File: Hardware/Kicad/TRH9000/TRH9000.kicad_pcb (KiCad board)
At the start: 2 copper layers, 99.1 x 63.5 mm, 74 parts, among them J1 RGB, J2 Console5_SCART, Q1 BC817, U1 V9990, U2 KM428C256, U3 KM428C256, U4 74VHC138, U5 T.I_SN74AHCT32D, U6 LMH1980, U7 T.I_SN74AHCT32D, X1 Crystek_CE3291, Y1 21.47727Mhz

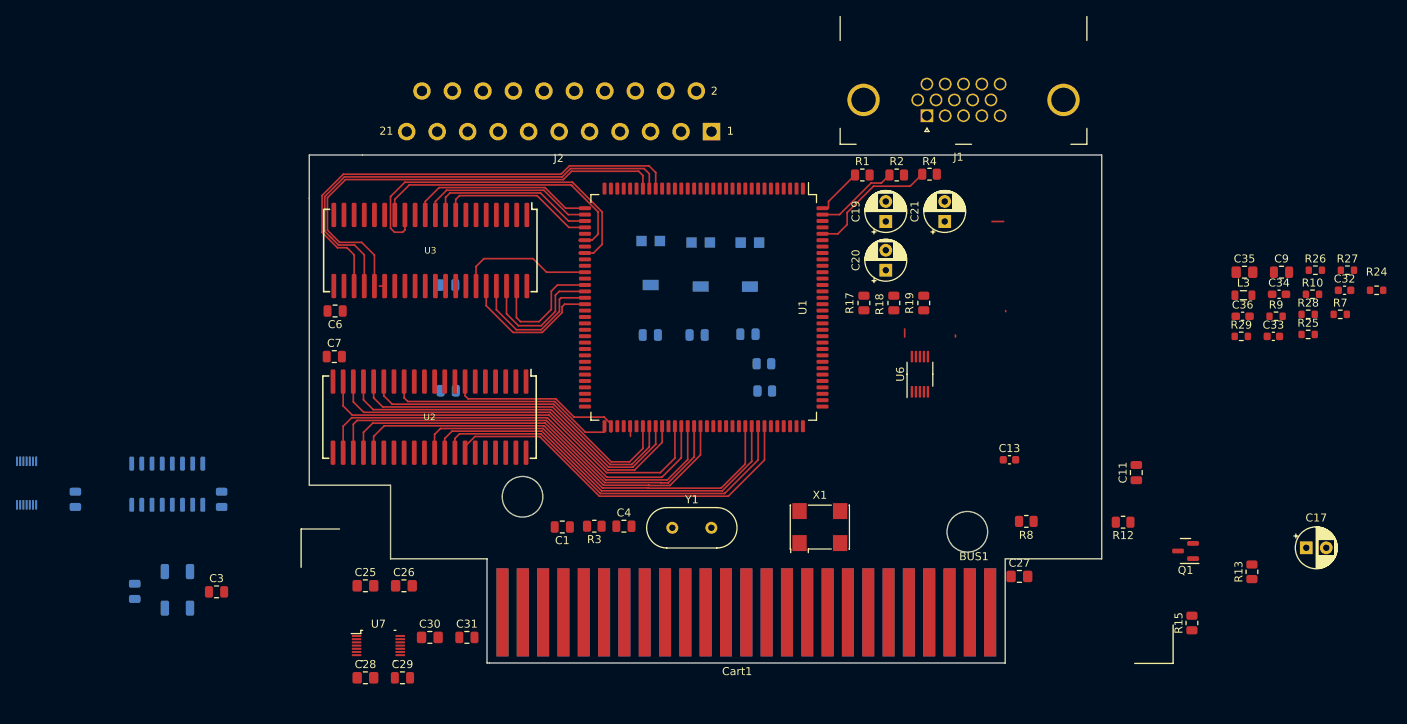
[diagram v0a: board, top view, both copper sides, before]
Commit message: Started routing the PCB, adding cut-outs to separate the analog from digital signal-domains.
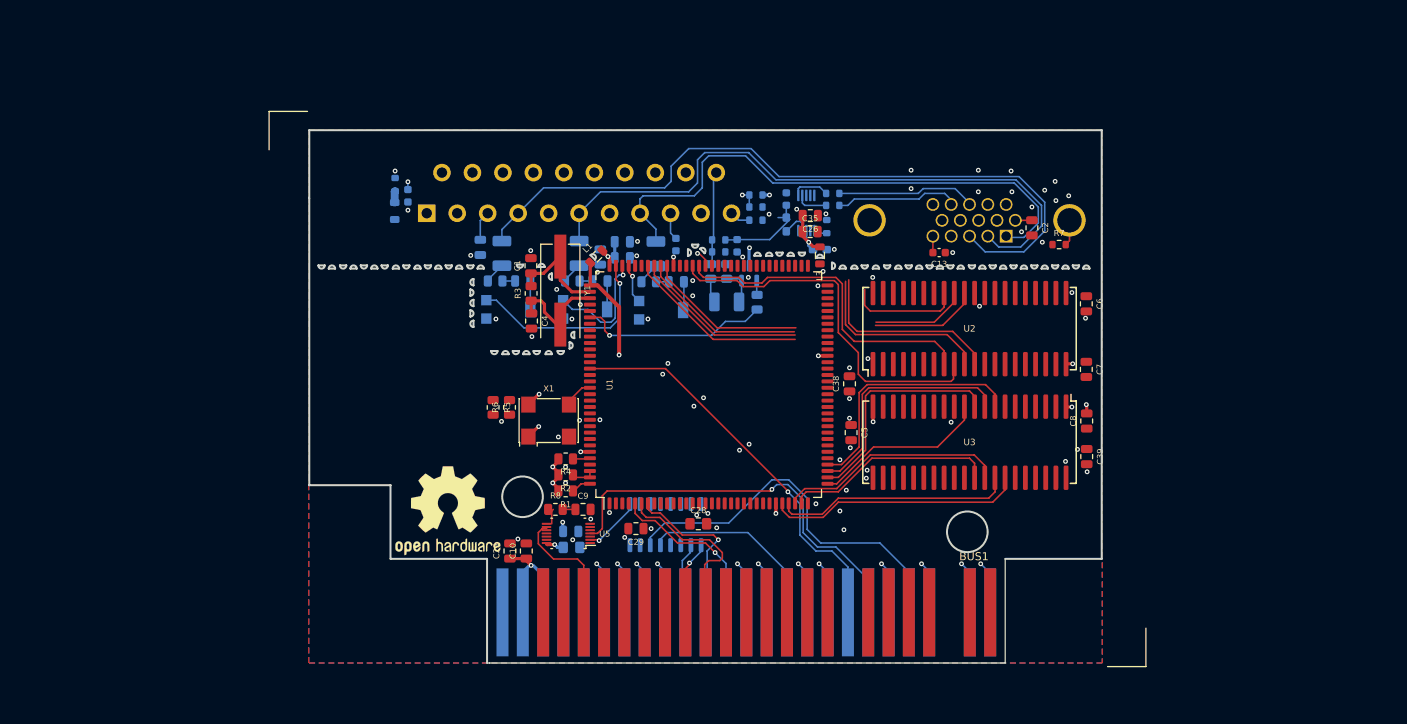
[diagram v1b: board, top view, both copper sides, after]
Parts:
- removed C11, C12: C_CC0805JPX7R9BB104, Capacitor_SMD:C_0805_2012Metric
- removed U7: T.I_SN74AHCT32D, trh9000:Texas_R-PDSO-G14_3.6x4.4mm
- added C23: C_CL21B106KOQNNNE, Capacitor_SMD:C_0805_2012Metric, F.Cu at (123.3, 113.0)
- added C24: C_CC0805JPX7R9BB104, Capacitor_SMD:C_0805_2012Metric, B.Cu at (119.7, 75.0)
- added C37: C_CC0805JPX7R9BB104, Capacitor_SMD:C_0805_2012Metric, B.Cu at (137.4, 74.3)
- added C38: C_CL21B106KOQNNNE, Capacitor_SMD:C_0805_2012Metric, F.Cu at (165.8, 92.1)
- added C39: C_CL21B106KOQNNNE, Capacitor_SMD:C_0805_2012Metric, F.Cu at (195.4, 101.2)
- added C40: 47pF, Capacitor_SMD:C_0603_1608Metric, B.Cu at (144.1, 74.7)
- added LOGO1: Logo_Open_Hardware_Small, Symbol:OSHW-Logo2_14.6x12mm_SilkScreen, F.Cu at (115.6, 108.0)
- added R11: R_ERJ-3GEYJ105V, Resistor_SMD:R_0603_1608Metric, B.Cu at (154.1, 71.7)
- BUS1: value MSX_SLOT_EDGE-CON -> MSX-CONN_L-P; footprint trh9000:msx_cartridge -> trh9000:msx_edge-conn-LP
- C10, C5, C8, R5, R6, U5: moved to F.Cu
- C17, C19, C20, C21: value 220uF -> C_TCJB227; footprint Capacitor_THT:CP_Radial_D5.0mm_P2.50mm -> Capacitor_Tantalum_SMD:CP_EIA-3528-15_AVX-H; moved to B.Cu
- C2: value 100nF -> C_CC0805JPX7R9BB104; moved to F.Cu
- C25: value C_CL21B105KBFNNNF -> C_GRM188D71A106KA73D; footprint Capacitor_SMD:C_0805_2012Metric_Pad1.18x1.45mm_HandSolder -> Capacitor_SMD:C_0603_1608Metric; moved to B.Cu
- C26: value C_CL21B105KBFNNNF -> 10nF; footprint Capacitor_SMD:C_0805_2012Metric_Pad1.18x1.45mm_HandSolder -> Capacitor_SMD:C_0805_2012Metric
- C27: value C_CL21B105KBFNNNF -> 10nF; footprint Capacitor_SMD:C_0805_2012Metric_Pad1.18x1.45mm_HandSolder -> Capacitor_SMD:C_0805_2012Metric; moved to B.Cu
- C3, C30, C31, C32, C33, C34, C36, J1, J2, Q1, R10, R12, R13, R15, R17, R18, R19, R24, R25, R26, R27, R28, R29, R9, U6: moved to B.Cu
- C35: value C_GRM21BR71A106KA73K -> C_CL21B106KOQNNNE; footprint Capacitor_SMD:C_0805_2012Metric_Pad1.18x1.45mm_HandSolder -> Capacitor_SMD:C_0805_2012Metric
- Cart1: footprint trh9000:MSX-cart-dummy -> trh9000:MSX-cart-dummy_RA
- L1: value 4.7uH -> L_MLZ2012M4R7HT000; footprint Inductor_SMD:L_1206_3216Metric -> Inductor_SMD:L_0805_2012Metric; moved to F.Cu
- L2: value 4.7uH -> L_MLZ2012M4R7HT000; footprint Inductor_SMD:L_1206_3216Metric -> Inductor_SMD:L_0805_2012Metric
- Y1: value 21.47727Mhz -> Y_HCM4921477270ABJT; footprint Crystal:Crystal_HC49-U_Vertical -> LRJ:Crystal_HC49-US_Vertical
- moved C2 121.0 mm to (188.6, 72.6), turned to -90 degrees
- moved R29 107.5 mm to (109.0, 67.2), turned to -90 degrees
- moved C7 94.0 mm to (195.4, 90.3), turned to -90 degrees
- moved C6 93.9 mm to (195.4, 82.1), turned to -90 degrees
- moved C9 92.2 mm to (132.5, 107.8)
- moved C8 79.9 mm to (195.4, 96.8), turned to 90 degrees
- moved C17 78.7 mm to (150.4, 81.9), turned to 180 degrees
- moved C32 76.1 mm to (151.8, 74.8), turned to -90 degrees
- moved R13 75.6 mm to (150.4, 78.1)
- moved R27 74.5 mm to (154.1, 68.5), turned to 180 degrees
- moved R10 74.5 mm to (149.4, 74.1), turned to 180 degrees
- moved R15 74.5 mm to (148.4, 78.1), turned to -90 degrees
- moved U3 71.5 mm to (180.8, 99.4)
- moved R28 70.3 mm to (154.1, 70.0)
- moved R9 70.1 mm to (149.4, 75.6)
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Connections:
- net /VDP/X1 renamed /VDP/X+
- net /VDP/X2 renamed /VDP/X-
- net /VIDEO/2.5V renamed /VIDEO/2.5VA
- net /VIDEO/SYNCIN renamed /VIDEO/Csync_
- net GND1 renamed /VIDEO/GNDD
- net Net-(C19-Pad1) renamed /VIDEO/RO_
- net Net-(C20-Pad1) renamed /VIDEO/GO_
- net Net-(C21-Pad1) renamed /VIDEO/BO_
- net Net-(R24-Pad2) renamed /VIDEO/REXT
- net Net-(R25-Pad2) renamed /VIDEO/HSOUT
- net Net-(R26-Pad2) renamed /VIDEO/VSOUT
- net Net-(U4-Pad9) renamed /~{Y6}
- C2 pad 1: +5VA -> /VIDEO/VGA_GND
- C2 pad 2: GNDA -> GND
- C25 pad 2: +12V -> Net-(C25-Pad2)
- C26 pad 1: -12V -> GND
- C26 pad 2: GND -> +5VA
- C27 pad 1: +5V -> GND
- C27 pad 2: GND -> +5VA
- C3 pad 2: GNDA -> GND
- J1 pad 6: GNDA -> /VIDEO/VGA_GND
- J1 pad 7: GNDA -> /VIDEO/VGA_GND
- J1 pad 8: GNDA -> /VIDEO/VGA_GND
- J2 pad 13: GNDA -> /VIDEO/Col_GND
- J2 pad 14: GND -> Net-(C25-Pad2)
- J2 pad 17: GNDA -> Net-(C40-Pad1)
- J2 pad 18: GND -> Net-(C25-Pad2)
- J2 pad 21: GND -> Net-(J2-Pad21)
- J2 pad 4: GNDA -> Net-(C25-Pad2)
- J2 pad 5: GNDA -> /VIDEO/Col_GND
- J2 pad 9: GNDA -> /VIDEO/Col_GND
- L2 pad 1: GND -> +12V
- L2 pad 2: GNDA -> +12VA
- Q1 pad 3: +5V -> +5VA
- R27 pad 1: +5V -> +5VA
- R29 pad 2: +12V -> +12VA
- U1 pad 92: GNDA -> GND
- U5 pad 14: (no net) -> +5V
- U5 pad 7: (no net) -> GND
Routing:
- net /VIDEO/BOUT: track 0.00 -> 92.8 mm
- net /VIDEO/GOUT: track 0.00 -> 79.8 mm
- net /VIDEO/ROUT: track 0.00 -> 69.5 mm
- net /VDP/V0A2: track 58.5 -> 0.00 mm
- net /VDP/V0A1: track 58.1 -> 0.00 mm
- net /VDP/V0A0: track 57.0 -> 0.00 mm
- net /VDP/V1A3: track 53.3 -> 0.00 mm
- net /VDP/V1A2: track 53.1 -> 0.00 mm
- net +5V: track 0.00 -> 52.0 mm, vias 0 -> 25
- net /VDP/V1A4: track 52.0 -> 0.00 mm
- net /VDP/V1A1: track 51.9 -> 0.00 mm
- net /~{WR}: track 0.00 -> 51.1 mm, vias 0 -> 1
- net /VDP/V1A0: track 50.9 -> 0.00 mm
- net /~{RESET}: track 0.00 -> 50.5 mm, vias 0 -> 1
- net /~{M1}: track 0.00 -> 48.4 mm
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- added copper zone on In2.Cu, net +5V
- added copper zone on In2.Cu, net +5VA
- added copper zone on In1.Cu, net /VIDEO/Col_GND
- added copper zone on B.Cu, net GND
- added copper zone on F.Cu, net GND
- added copper zone on In1.Cu, net GND
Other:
- board size 99.1 x 63.5 mm -> 99.1 x 66.6 mm
- copper layers 2 -> 4

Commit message: More routing of the analog portion. Added 3D-models for the VGA and Scart connectors.
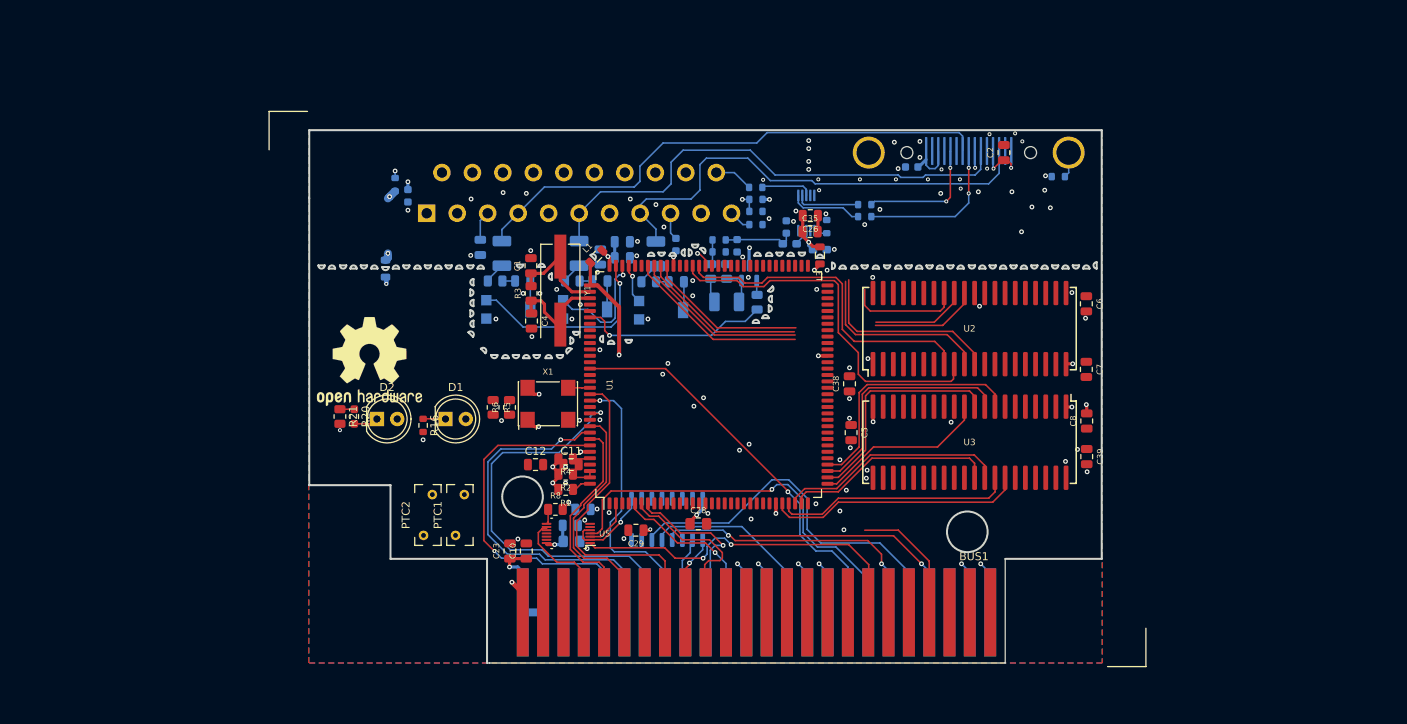
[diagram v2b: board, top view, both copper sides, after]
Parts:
- added C11: C_CC0805JPX7R9BB104, Capacitor_SMD:C_0805_2012Metric, F.Cu at (131.0, 102.2)
- added C12: C_CL21B106KOQNNNE, Capacitor_SMD:C_0805_2012Metric, F.Cu at (126.5, 102.2)
- added D1: SunLED_XCVG12D, LED_THT:LED_D5.0mm, F.Cu at (115.3, 96.5)
- added D2: LO_LED_LTL2R3K, LED_THT:LED_D5.0mm, F.Cu at (106.7, 96.5)
- added PTC1: F_0ZRC0025FF1E, LRJ:Fuse_BelFuse_0ZRC0025FF_L7.4mm_W3.1mm, F.Cu at (117.1, 108.5)
- added PTC2: F_0ZRC0025FF1E, LRJ:Fuse_BelFuse_0ZRC0025FF_L7.4mm_W3.1mm, F.Cu at (113.1, 108.5)
- added R14: 75, Resistor_SMD:R_0603_1608Metric, B.Cu at (154.1, 67.5)
- added R16: 120R, Resistor_SMD:R_0603_1608Metric, F.Cu at (112.5, 97.3)
- added R20: R_RT0603BRE075KL, Resistor_SMD:R_0603_1608Metric_Pad0.98x0.95mm_HandSolder, F.Cu at (103.9, 96.2)
- added R21: 100R, Resistor_SMD:R_0805_2012Metric, F.Cu at (102.1, 96.2)
- BUS1: footprint trh9000:msx_edge-conn-LP -> trh9000:msx_cart_edge-conn
- C13, C9, R7: moved to B.Cu
- J1: value RGB -> Norcomp_200-015-263R001; footprint LRJ:DSUB-Amphenol_L77HDE15SD1CH4RHNVGA -> LRJ:Norcomp_DSUB-15-HD_Female_Horizontal_SMD_P0.77x1.98mm
- moved LOGO1 21.1 mm to (105.8, 89.3)
- moved C13 11.2 mm to (173.6, 65.0), turned to 0 degrees
- moved C2 10.0 mm to (185.1, 63.2), turned to 90 degrees
- moved R7 8.50 mm to (191.9, 66.2)
- moved L2 7.29 mm to (107.8, 77.7)
- moved J1 6.30 mm to (180.7, 59.8)
- moved R25 4.94 mm to (167.7, 71.2)
- moved R26 4.00 mm to (167.7, 69.7)
- moved C33 3.50 mm to (157.9, 72.5)
- moved C34 2.45 mm to (158.3, 74.6), turned to 180 degrees
- moved X1 2.10 mm to (128.1, 94.6)
- moved C31 0.75 mm to (130.9, 109.8)
- moved C30 0.75 mm to (131.1, 111.8)
- moved U4 0.68 mm to (143.0, 109.0)
- moved R11 0.55 mm to (154.1, 72.2)
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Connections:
- net /SW1 renamed /MSX_SW1
- net /SW2 renamed /MSX_SW2
- net /VIDEO/Csync_ renamed /VIDEO/~{CSYNCA_}
- net Net-(C25-Pad2) renamed /VIDEO/AUGND
- C28 pad 1: +5V -> +5VP
- C29 pad 1: +5V -> +5VP
- C30 pad 1: +5V -> +5VP
- C31 pad 1: +5V -> +5VP
- C38 pad 1: +5V -> +5VP
- C39 pad 1: +5V -> +5VP
- C5 pad 1: +5V -> +5VP
- C6 pad 2: +5V -> +5VP
- C7 pad 1: +5V -> +5VP
- C8 pad 2: +5V -> +5VP
- J2 pad 20: /VIDEO/CSYNCO -> /VIDEO/~{CSYNCO}
- L1 pad 1: +5V -> +5VP
- L2 pad 1: +12V -> /Power/12VP
- L3 pad 1: +5V -> +5VP
- R1 pad 1: +5V -> +5VP
- R10 pad 2: /VIDEO/CSYNCO -> /VIDEO/~{CSYNCA}
- R15 pad 1: /VIDEO/CSYNCO -> /VIDEO/~{CSYNCA}
- R2 pad 1: +5V -> +5VP
- R4 pad 1: +5V -> +5VP
- R5 pad 1: +5V -> +5VP
- R6 pad 2: +5V -> +5VP
- R9 pad 1: /VIDEO/CSYNCO -> /VIDEO/~{CSYNCA}
- U1 pad 123: +5V -> +5VP
- U1 pad 27: +5V -> +5VP
- U1 pad 53: +5V -> +5VP
- U1 pad 81: +5V -> +5VP
- U1 pad 97: +5V -> +5VP
- U2 pad 1: +5V -> +5VP
- U2 pad 20: +5V -> +5VP
- U3 pad 1: +5V -> +5VP
- U3 pad 20: +5V -> +5VP
- U4 pad 16: +5V -> +5VP
- U5 pad 14: +5V -> +5VP
- U6 pad 8: unconnected-(U6-Pad8) -> /VIDEO/CSOUT
- X1 pad 1: +5V -> +5VP
- X1 pad 4: +5V -> +5VP
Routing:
- net /D3: track 6.49 -> 52.8 mm
- net /VIDEO/AUGND: track 46.3 -> 1.53 mm
- net /~{RD}: track 0.00 -> 44.6 mm, vias 0 -> 2
- net +5VP: track 0.00 -> 42.4 mm, vias 0 -> 18
- net /D5: track 6.43 -> 47.5 mm
- net /D0: track 0.00 -> 40.9 mm
- net +5V: track 52.0 -> 12.6 mm, vias 25 -> 7
- net /D7: track 6.45 -> 45.9 mm
- net /D4: track 0.00 -> 30.9 mm
- net /Power/12VP: track 0.00 -> 29.6 mm, vias 0 -> 1
- net /~{IORQ}: track 6.44 -> 36.0 mm, vias 1 -> 2
- net /D1: track 6.46 -> 35.7 mm
- net /D6: track 0.00 -> 27.6 mm
- net /VIDEO/BOUT: track 92.8 -> 67.2 mm
- net /~{WAIT}: track 8.95 -> 33.0 mm
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- added copper zone on In2.Cu, net +5VP
- added copper zone on In1.Cu, net /VIDEO/AUGND
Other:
- outline, holes or cut-outs redrawn
